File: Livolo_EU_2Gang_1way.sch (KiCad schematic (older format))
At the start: 38 parts, among them IC1 ATMEGA328P, U1 ATSHA204A, U2 NRF24L01, U6 Touch, U7 Touch, U8 MTCH105

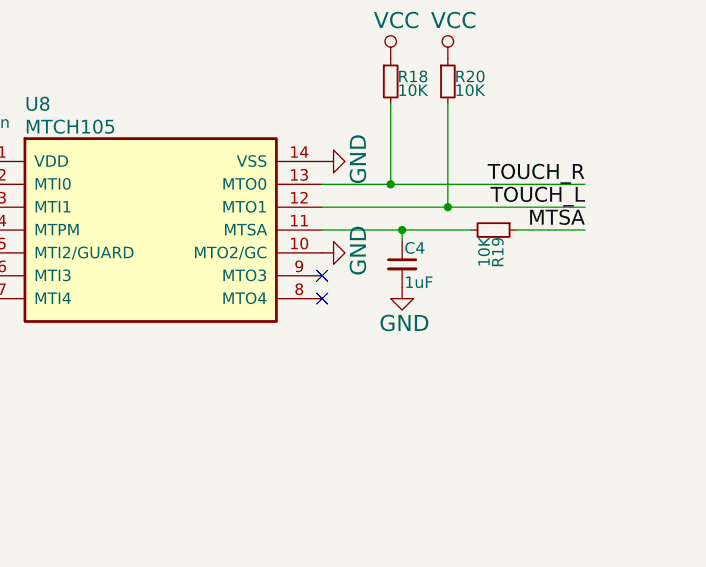
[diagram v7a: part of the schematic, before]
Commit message: adding shunt for test with or without guard
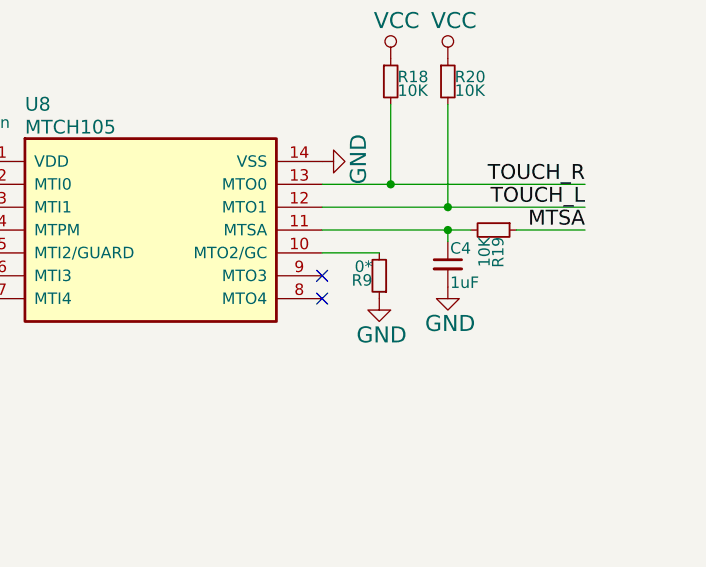
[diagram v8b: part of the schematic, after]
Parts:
- added R9: 0*, Resistors_SMD:R_0603, symbol R_Small
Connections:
- net GND: now also R9.1; no longer U8.10 (MTO2/GC)
- new net: R9.2, U8.10 (MTO2/GC)
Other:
- moved on the sheet: C4
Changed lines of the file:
@@
 L GND #GND018
 U 1 1 597C94D4
-P 14500 2900
-F 0 "#GND018" H 14400 2800 70  0001 L BNN
-F 1 "GND" H 14400 2700 70  0000 L BNN
-F 2 "" H 14500 2900 60  0001 C CNN
-F 3 "" H 14500 2900 60  0001 C CNN
-	1    14500 2900
-	0    -1   -1   0
+P 14750 3100
+F 0 "#GND018" H 14650 3000 70  0001 L BNN
+F 1 "GND" H 14650 2900 70  0000 L BNN
+F 2 "" H 14750 3100 60  0001 C CNN
+F 3 "" H 14750 3100 60  0001 C CNN
+	1    14750 3100
+	1    0    0    -1
 $EndComp
 $Comp
@@
 L GND #GND022
 U 1 1 597D1D52
-P 14850 3050
-F 0 "#GND022" H 14750 2950 70  0001 L BNN
-F 1 "GND" H 14750 2850 70  0000 L BNN
-F 2 "" H 14850 3050 60  0001 C CNN
-F 3 "" H 14850 3050 60  0001 C CNN
-	1    14850 3050
+P 15050 3050
+F 0 "#GND022" H 14950 2950 70  0001 L BNN
+F 1 "GND" H 14950 2850 70  0000 L BNN
+F 2 "" H 15050 3050 60  0001 C CNN
+F 3 "" H 15050 3050 60  0001 C CNN
+	1    15050 3050
 	1    0    0    -1
 $EndComp
@@
 L C_Small C4
 U 1 1 597D87A2
-P 14850 2950
-F 0 "C4" H 14860 3020 50  0000 L CNN
-F 1 "1uF" H 14860 2870 50  0000 L CNN
-F 2 "Capacitors_SMD:C_0603_HandSoldering" H 14850 2950 50  0001 C CNN
-F 3 "" H 14850 2950 50  0001 C CNN
-	1    14850 2950
+P 15050 2950
+F 0 "C4" H 15060 3020 50  0000 L CNN
+F 1 "1uF" H 15060 2870 50  0000 L CNN
+F 2 "Capacitors_SMD:C_0603_HandSoldering" H 15050 2950 50  0001 C CNN
+F 3 "" H 15050 2950 50  0001 C CNN
+	1    15050 2950
 	1    0    0    -1
 $EndComp
@@
 	14500 2700 15650 2700
 Wire Wire Line
-	14500 2800 15150 2800
-Wire Wire Line
 	15350 2800 15650 2800
 Wire Wire Line
@@
 	12950 2350 12950 2500
 Connection ~ 12950 2500
-Connection ~ 14850 2800
-Wire Wire Line
-	14850 2800 14850 2850
+Connection ~ 15050 2800
+Wire Wire Line
+	15050 2800 15050 2850
 Wire Wire Line
 	13000 2800 12900 2800
@@
 Wire Wire Line
 	12700 2600 13000 2600
+Wire Wire Line
+	15150 2800 14500 2800
+$Comp
+L R_Small R9
+U 1 1 597CCC76
+P 14750 3000
+F 0 "R9" H 14780 3020 50  0000 L CNN
+F 1 "0*" H 14780 2960 50  0000 L CNN
+F 2 "Resistors_SMD:R_0603" H 14750 3000 50  0001 C CNN
+F 3 "" H 14750 3000 50  0001 C CNN
+	1    14750 3000
+	-1   0    0    1
+$EndComp
+Wire Wire Line
+	14750 2900 14500 2900
 $EndSCHEMATC
